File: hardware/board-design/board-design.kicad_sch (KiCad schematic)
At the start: 1 part, among them J1 Conn_01x02_Pin

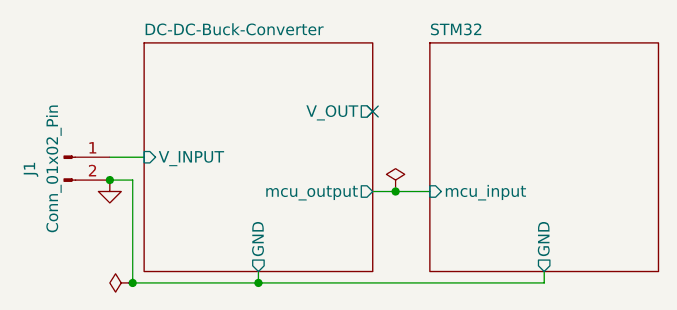
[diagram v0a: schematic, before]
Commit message: feat(schematic): redesign buck converter circuit
Replaced the gate driver and regulator stage with a dedicated Buck Controller IC to resolve missing feedback loops and completed the schematic redesign.
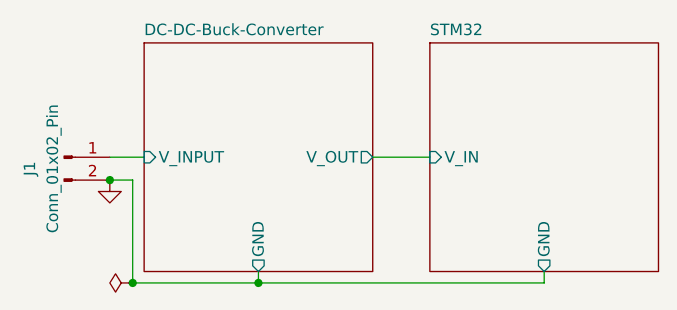
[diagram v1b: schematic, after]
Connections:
- no-connect marks 1 -> 0
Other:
- sheet DC-DC-Buck-Converter ports: added none; removed mcu_output
- sheet STM32 ports: added V_IN; removed mcu_input
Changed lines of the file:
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@@
 	(paper "A4")
+	(junction
+		(at 116.84 106.68)
+		(diameter 0)
+		(color 0 0 0 0)
+	)
 	(junction
 		(at 119.38 118.11)
@@
 	)
 	(junction
-		(at 148.59 107.95)
-		(diameter 0)
-		(color 0 0 0 0)
-	)
-	(junction
-		(at 116.84 106.68)
-		(diameter 0)
-		(color 0 0 0 0)
-	)
-	(junction
 		(at 133.35 118.11)
 		(diameter 0)
 		(color 0 0 0 0)
 	)
-	(no_connect
-		(at 146.05 99.06)
-	)
 	(wire
 		(pts
@@
 	(wire
 		(pts
-			(xy 146.05 107.95) (xy 148.59 107.95)
+			(xy 146.05 104.14) (xy 152.4 104.14)
 		)
 		(stroke
@@
 		(pts
 			(xy 165.1 118.11) (xy 165.1 116.84)
-		)
-		(stroke
-			(width 0)
-			(type default)
-		)
-	)
-	(wire
-		(pts
-			(xy 148.59 107.95) (xy 152.4 107.95)
 		)
 		(stroke
@@
 		)
 	)
-	(symbol
-		(lib_id "power:PWR_FLAG")
-		(at 148.59 107.95 0)
-		(unit 1)
-		(body_style 1)
-		(exclude_from_sim no)
-		(in_bom yes)
-		(on_board yes)
-		(in_pos_files yes)
-		(dnp no)
-		(fields_autoplaced yes)
-		(property "Reference" "#FLG03"
-			(at 148.59 106.045 0)
-			(hide yes)
-			(show_name no)
-			(do_not_autoplace no)
-			(effects
-				(font
-					(size 1.27 1.27)
-				)
-			)
-		)
-		(property "Value" "PWR_FLAG"
-			(at 148.5899 104.14 90)
-			(hide yes)
-			(show_name no)
-			(do_not_autoplace no)
-			(effects
-				(font
-					(size 1.27 1.27)
-				)
-				(justify left)
-			)
-		)
-		(property "Footprint" ""
-			(at 148.59 107.95 0)
-			(hide yes)
-			(show_name no)
-			(do_not_autoplace no)
-			(effects
-				(font
-					(size 1.27 1.27)
-				)
-			)
-		)
-		(property "Datasheet" ""
-			(at 148.59 107.95 0)
-			(hide yes)
-			(show_name no)
-			(do_not_autoplace no)
-			(effects
-				(font
-					(size 1.27 1.27)
-				)
-			)
-		)
-		(property "Description" "Special symbol for telling ERC where power comes from"
-			(at 148.59 107.95 0)
-			(hide yes)
-			(show_name no)
-			(do_not_autoplace no)
-			(effects
-				(font
-					(size 1.27 1.27)
-				)
-			)
-		)
-		(pin "1"
-		)
-		(instances
-			(project "board-design"
-				(path "/bd5d7a3e-3306-4abd-ba38-3ca87df9a9fb"
-					(reference "#FLG03")
-					(unit 1)
-				)
-			)
-		)
-	)
 	(sheet
 		(at 120.65 91.44)
@@
 		)
 		(pin "V_OUT" output
-			(at 146.05 99.06 0)
+			(at 146.05 104.14 0)
 			(effects
 				(font
@@
 				)
 				(justify left)
-			)
-		)
-		(pin "mcu_output" output
-			(at 146.05 107.95 0)
-			(effects
-				(font
-					(size 1.27 1.27)
-				)
-				(justify right)
 			)
 		)
@@
 			)
 		)
-		(pin "mcu_input" input
-			(at 152.4 107.95 180)
-			(effects
-				(font
+		(pin "V_IN" input
+			(at 152.4 104.14 180)
+			(effects
+				(font
